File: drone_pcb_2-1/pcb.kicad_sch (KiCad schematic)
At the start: 3 parts, among them U1 MPU-6050, U3 ESP32-WROOM-32

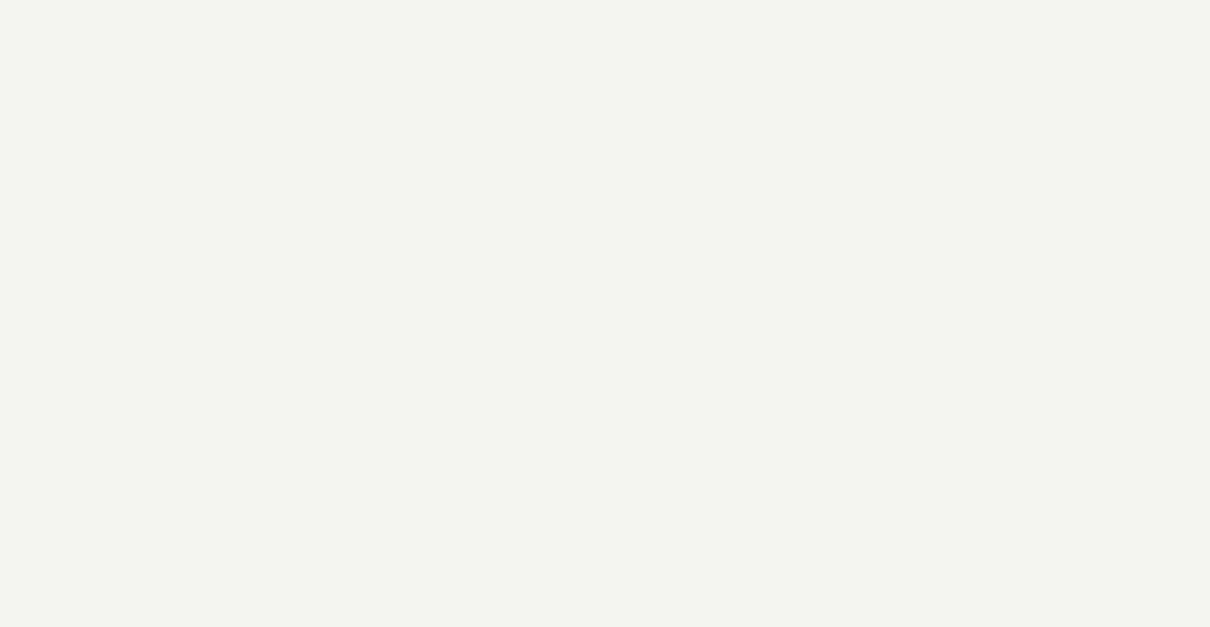
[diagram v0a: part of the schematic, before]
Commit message: add A5936 esc
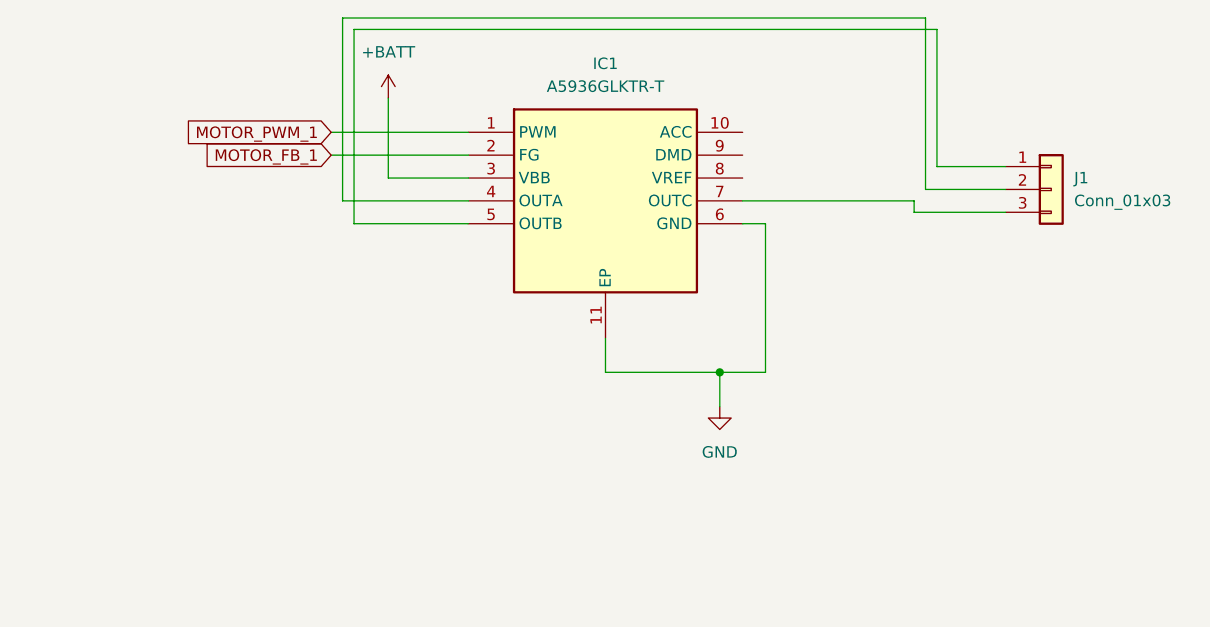
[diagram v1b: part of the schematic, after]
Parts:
- added IC1: A5936GLKTR-T, SOP100P600X165-11N, symbol A5936:A5936GLKTR-T
- added J1: Conn_01x03, symbol Connector_Generic:Conn_01x03
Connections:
- new net: IC1.5 (OUTB), J1.1 (Pin_1)
- new net: IC1.4 (OUTA), J1.2 (Pin_2)
- new net: IC1.7 (OUTC), J1.3 (Pin_3)
- new net +BATT: IC1.3 (VBB)
- new net GND: IC1.11 (EP), IC1.6 (GND)
- new net MOTOR_FB_1: IC1.2 (FG)
- new net MOTOR_PWM_1: IC1.1 (PWM)
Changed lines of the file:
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@@
 (kicad_sch (version 20230121) (generator eeschema)
   (paper "A3")
+  (junction (at 355.6 67.31) (diameter 0) (color 0 0 0 0)
+  )
+  (wire (pts (xy 313.69 27.94) (xy 378.46 27.94))
+    (stroke (width 0) (type default))
+  )
+  (wire (pts (xy 377.19 49.53) (xy 387.35 49.53))
+    (stroke (width 0) (type default))
+  )
+  (wire (pts (xy 378.46 27.94) (xy 378.46 46.99))
+    (stroke (width 0) (type default))
+  )
+  (wire (pts (xy 312.42 40.64) (xy 327.66 40.64))
+    (stroke (width 0) (type default))
+  )
+  (wire (pts (xy 379.73 29.21) (xy 379.73 44.45))
+    (stroke (width 0) (type default))
+  )
+  (wire (pts (xy 312.42 43.18) (xy 327.66 43.18))
+    (stroke (width 0) (type default))
+  )
+  (wire (pts (xy 314.96 50.8) (xy 314.96 29.21))
+    (stroke (width 0) (type default))
+  )
+  (wire (pts (xy 378.46 46.99) (xy 387.35 46.99))
+    (stroke (width 0) (type default))
+  )
+  (wire (pts (xy 327.66 50.8) (xy 314.96 50.8))
+    (stroke (width 0) (type default))
+  )
+  (wire (pts (xy 358.14 50.8) (xy 360.68 50.8))
+    (stroke (width 0) (type default))
+  )
+  (wire (pts (xy 327.66 48.26) (xy 313.69 48.26))
+    (stroke (width 0) (type default))
+  )
+  (wire (pts (xy 313.69 48.26) (xy 313.69 27.94))
+    (stroke (width 0) (type default))
+  )
+  (wire (pts (xy 327.66 45.72) (xy 318.77 45.72))
+    (stroke (width 0) (type default))
+  )
+  (wire (pts (xy 377.19 48.26) (xy 377.19 49.53))
+    (stroke (width 0) (type default))
+  )
+  (wire (pts (xy 342.9 63.5) (xy 342.9 67.31))
+    (stroke (width 0) (type default))
+  )
+  (wire (pts (xy 318.77 45.72) (xy 318.77 36.83))
+    (stroke (width 0) (type default))
+  )
+  (wire (pts (xy 379.73 44.45) (xy 387.35 44.45))
+    (stroke (width 0) (type default))
+  )
+  (wire (pts (xy 355.6 71.12) (xy 355.6 67.31))
+    (stroke (width 0) (type default))
+  )
+  (wire (pts (xy 358.14 48.26) (xy 377.19 48.26))
+    (stroke (width 0) (type default))
+  )
+  (wire (pts (xy 314.96 29.21) (xy 379.73 29.21))
+    (stroke (width 0) (type default))
+  )
+  (wire (pts (xy 342.9 67.31) (xy 355.6 67.31))
+    (stroke (width 0) (type default))
+  )
+  (wire (pts (xy 360.68 67.31) (xy 355.6 67.31))
+    (stroke (width 0) (type default))
+  )
+  (wire (pts (xy 360.68 50.8) (xy 360.68 67.31))
+    (stroke (width 0) (type default))
+  )
+  (global_label "MOTOR_PWM_1" (shape input) (at 312.42 40.64 180) (fields_autoplaced)
+    (effects (font (size 1.27 1.27)) (justify right))
+    (property "Intersheetrefs" "${INTERSHEET_REFS}" (at 295.8467 40.64 0)
+      (effects (font (size 1.27 1.27)) (justify right) hide)
+    )
+  )
+  (global_label "MOTOR_FB_1" (shape input) (at 312.42 43.18 180) (fields_autoplaced)
+    (effects (font (size 1.27 1.27)) (justify right))
+    (property "Intersheetrefs" "${INTERSHEET_REFS}" (at 297.6609 43.18 0)
+      (effects (font (size 1.27 1.27)) (justify right) hide)
+    )
+  )
+  (symbol (lib_id "Connector_Generic:Conn_01x03") (at 392.43 46.99 0) (unit 1)
+    (in_bom yes) (on_board yes) (dnp no) (fields_autoplaced)
+    (property "Reference" "J1" (at 394.97 45.72 0)
+      (effects (font (size 1.27 1.27)) (justify left))
+    )
+    (property "Value" "Conn_01x03" (at 394.97 48.26 0)
+      (effects (font (size 1.27 1.27)) (justify left))
+    )
+    (property "Footprint" "" (at 392.43 46.99 0)
+      (effects (font (size 1.27 1.27)) hide)
+    )
+    (property "Datasheet" "~" (at 392.43 46.99 0)
+      (effects (font (size 1.27 1.27)) hide)
+    )
+    (pin "1")
+    (pin "2")
+    (pin "3")
+    (instances
+      (project "pcb"
+        (path "/86dd2ef4-708d-4533-9384-626d9620d24d"
+          (reference "J1") (unit 1)
+        )
+      )
+    )
+  )
   (symbol (lib_id "RF_Module:DWM1000") (at 72.39 73.66 0) (unit 1)
     (in_bom yes) (on_board yes) (dnp no) (fields_autoplaced)
@@
         (path "/86dd2ef4-708d-4533-9384-626d9620d24d"
           (reference "DWM1") (unit 1)
+        )
+      )
+    )
+  )
+  (symbol (lib_id "power:+BATT") (at 318.77 36.83 0) (unit 1)
+    (in_bom yes) (on_board yes) (dnp no) (fields_autoplaced)
+    (property "Reference" "#PWR02" (at 318.77 40.64 0)
+      (effects (font (size 1.27 1.27)) hide)
+    )
+    (property "Value" "+BATT" (at 318.77 31.75 0)
+      (effects (font (size 1.27 1.27)))
+    )
+    (property "Footprint" "" (at 318.77 36.83 0)
+      (effects (font (size 1.27 1.27)) hide)
+    )
+    (property "Datasheet" "" (at 318.77 36.83 0)
+      (effects (font (size 1.27 1.27)) hide)
+    )
+    (pin "1")
+    (instances
+      (project "pcb"
+        (path "/86dd2ef4-708d-4533-9384-626d9620d24d"
+          (reference "#PWR02") (unit 1)
         )
       )
@@
         )
       )
+    )
+  )
+  (symbol (lib_id "A5936:A5936GLKTR-T") (at 327.66 40.64 0) (unit 1)
+    (in_bom yes) (on_board yes) (dnp no) (fields_autoplaced)
+    (property "Reference" "IC1" (at 342.9 33.02 0)
+      (effects (font (size 1.27 1.27)))
+    )
+    (property "Value" "A5936GLKTR-T" (at 342.9 35.56 0)
+      (effects (font (size 1.27 1.27)))
+    )
+    (property "Footprint" "SOP100P600X165-11N" (at 354.33 135.56 0)
+      (effects (font (size 1.27 1.27)) (justify left top) hide)
+    )
+    (property "Datasheet" "https://www.allegromicro.com/-/media/files/datasheets/a5936-datasheet.ashx" (at 354.33 235.56 0)
+      (effects (font (size 1.27 1.27)) (justify left top) hide)
+    )
+    (property "Height" "1.65" (at 354.33 435.56 0)
+      (effects (font (size 1.27 1.27)) (justify left top) hide)
+    )
+    (property "Manufacturer_Name" "Allegro Microsystems" (at 354.33 535.56 0)
+      (effects (font (size 1.27 1.27)) (justify left top) hide)
+    )
+    (property "Manufacturer_Part_Number" "A5936GLKTR-T" (at 354.33 635.56 0)
+      (effects (font (size 1.27 1.27)) (justify left top) hide)
+    )
+    (property "Mouser Part Number" "" (at 354.33 735.56 0)
+      (effects (font (size 1.27 1.27)) (justify left top) hide)
+    )
+    (property "Mouser Price/Stock" "" (at 354.33 835.56 0)
+      (effects (font (size 1.27 1.27)) (justify left top) hide)
+    )
+    (property "Arrow Part Number" "" (at 354.33 935.56 0)
+      (effects (font (size 1.27 1.27)) (justify left top) hide)
+    )
+    (property "Arrow Price/Stock" "" (at 354.33 1035.56 0)
+      (effects (font (size 1.27 1.27)) (justify left top) hide)
+    )
+    (pin "1")
+    (pin "10")
+    (pin "11")
+    (pin "2")
+    (pin "3")
+    (pin "4")
+    (pin "5")
+    (pin "6")
+    (pin "7")
+    (pin "8")
+    (pin "9")
+    (instances
+      (project "pcb"
+        (path "/86dd2ef4-708d-4533-9384-626d9620d24d"
+          (reference "IC1") (unit 1)
+        )
+      )
+    )
+  )
+  (symbol (lib_id "power:GND") (at 355.6 71.12 0) (unit 1)
+    (in_bom yes) (on_board yes) (dnp no) (fields_autoplaced)
+    (property "Reference" "#PWR01" (at 355.6 77.47 0)
+      (effects (font (size 1.27 1.27)) hide)
+    )
+    (property "Value" "GND" (at 355.6 76.2 0)
+      (effects (font (size 1.27 1.27)))
+    )
+    (property "Footprint" "" (at 355.6 71.12 0)
+      (effects (font (size 1.27 1.27)) hide)
+    )
+    (property "Datasheet" "" (at 355.6 71.12 0)
+      (effects (font (size 1.27 1.27)) hide)
+    )
+    (pin "1")
+    (instances
+      (project "pcb"
+        (path "/86dd2ef4-708d-4533-9384-626d9620d24d"
+          (reference "#PWR01") (unit 1)
+        )
+      )

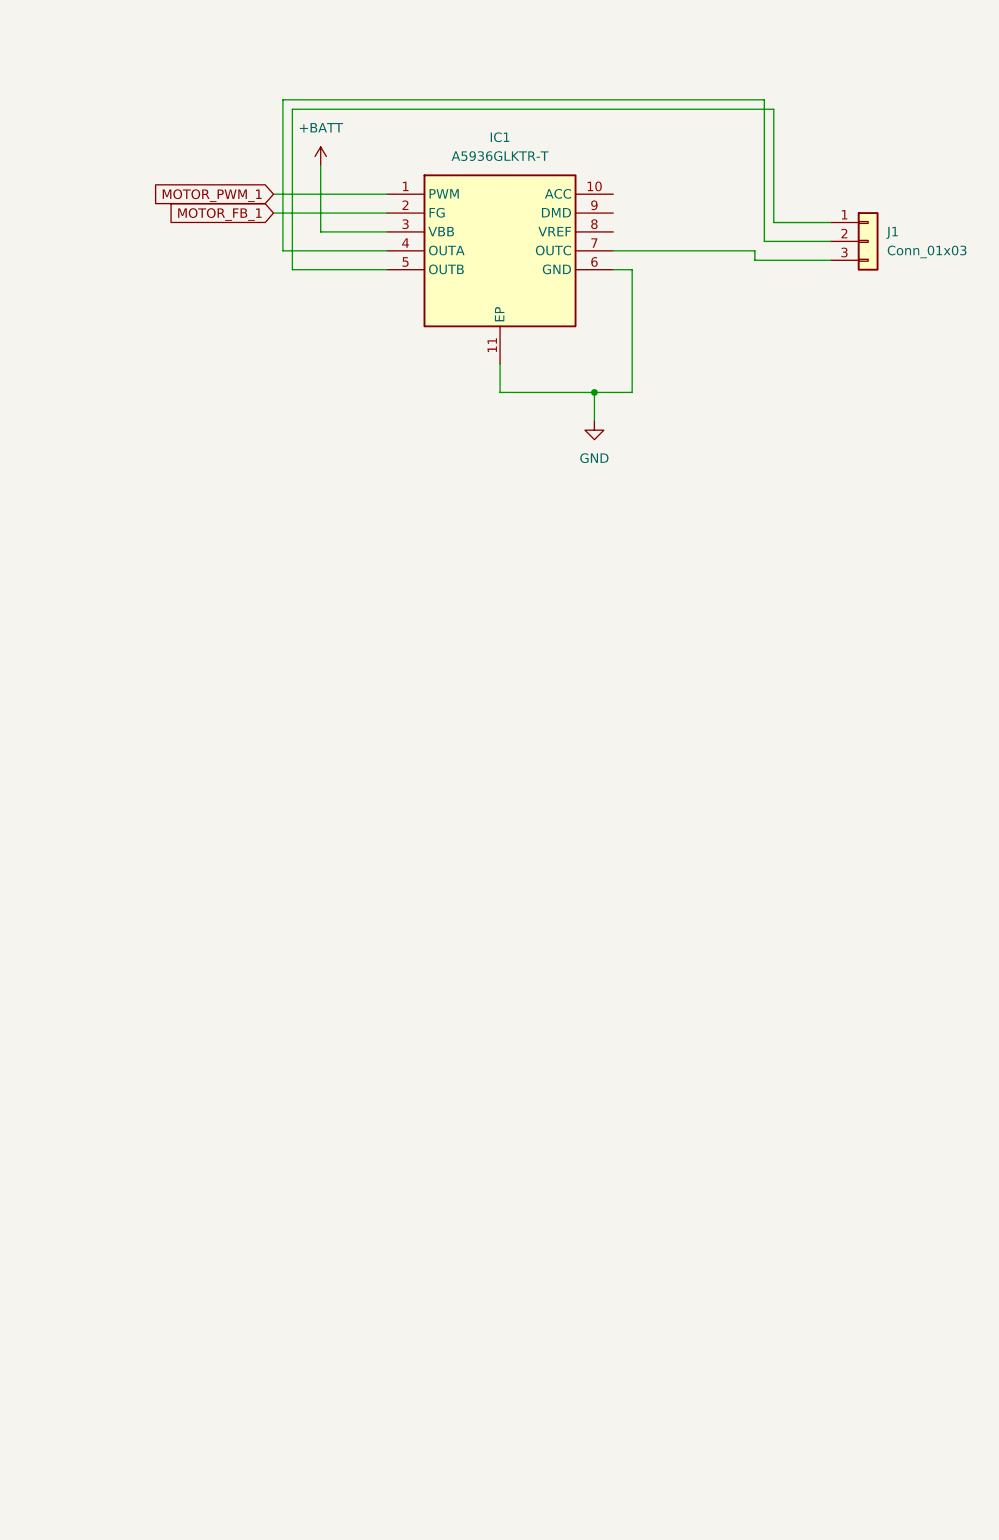
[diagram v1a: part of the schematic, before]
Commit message: add motor esc
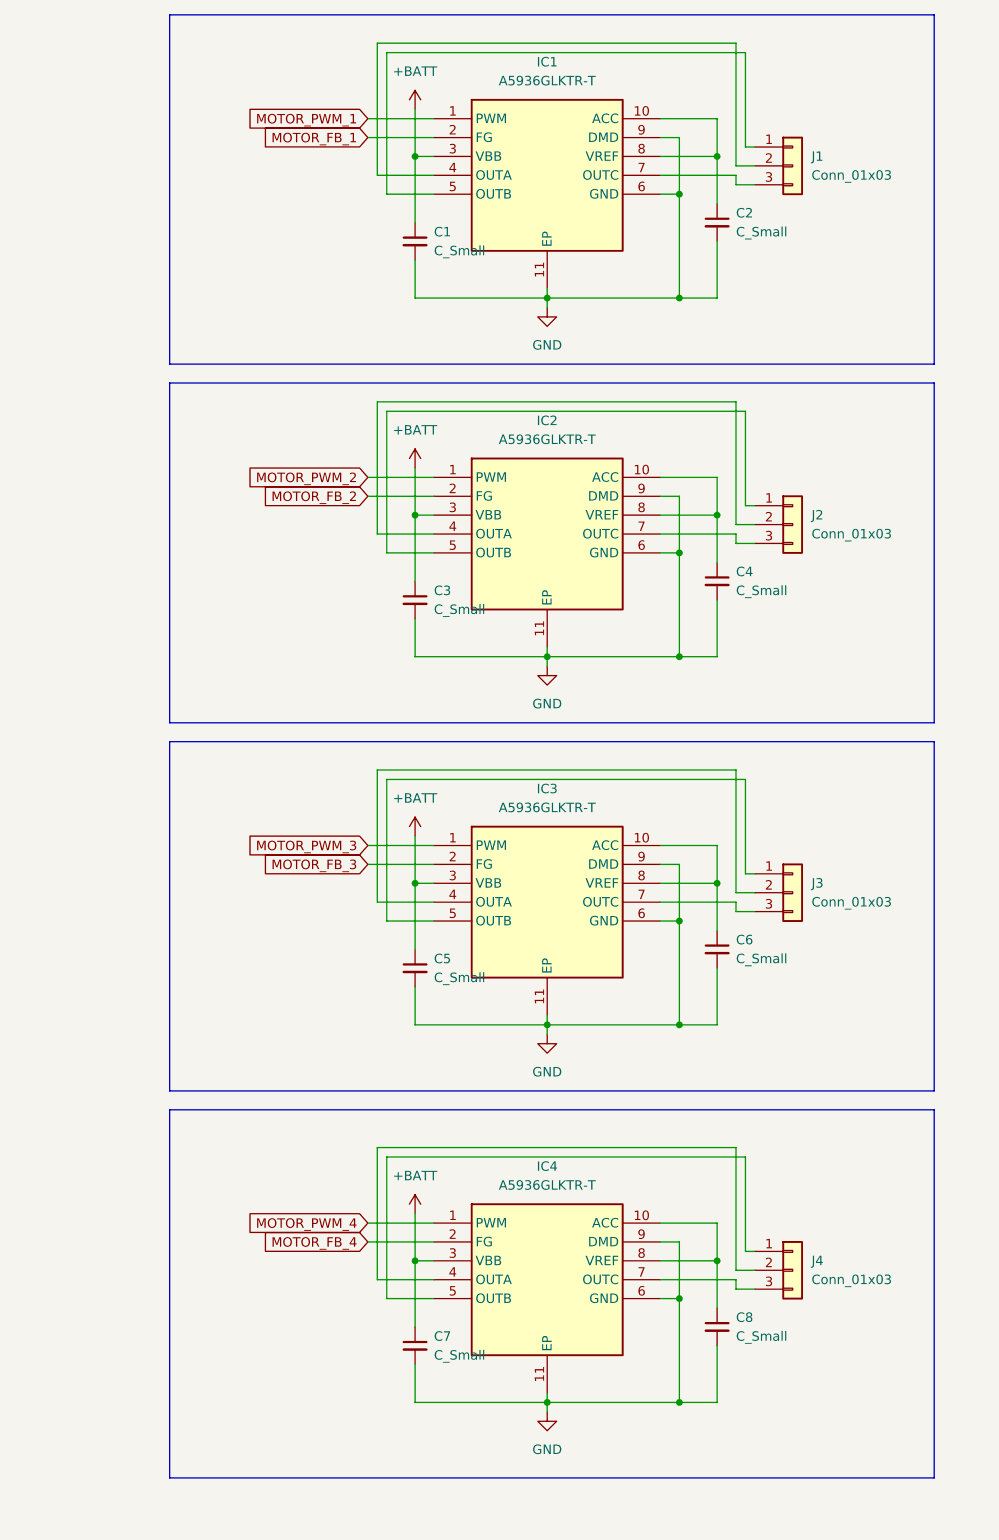
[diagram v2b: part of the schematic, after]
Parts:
- added C1, C2, C3, C4, C5, C6, C7, C8: C_Small, symbol Device:C_Small
- added IC2, IC3, IC4: A5936GLKTR-T, SOP100P600X165-11N, symbol A5936:A5936GLKTR-T
- added J2, J3, J4: Conn_01x03, symbol Connector_Generic:Conn_01x03
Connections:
- net +BATT: now also C1.1, C3.1, C5.1, C7.1, IC2.3 (VBB), IC3.3 (VBB), IC4.3 (VBB)
- net GND: now also IC1.9 (DMD), C1.2, C2.2, C3.2, C4.2, C5.2, C6.2, C7.2, C8.2, IC2.11 (EP), IC2.6 (GND), IC2.9 (DMD), IC3.11 (EP), IC3.6 (GND), IC3.9 (DMD), IC4.11 (EP), IC4.6 (GND), IC4.9 (DMD)
- net at IC1.10 (ACC): now also IC1.8 (VREF), C2.1
- new net: C4.1, IC2.10 (ACC), IC2.8 (VREF)
- new net: IC2.4 (OUTA), J2.2 (Pin_2)
- new net: IC2.5 (OUTB), J2.1 (Pin_1)
- new net: IC2.7 (OUTC), J2.3 (Pin_3)
- new net: C8.1, IC4.10 (ACC), IC4.8 (VREF)
- new net: IC4.4 (OUTA), J4.2 (Pin_2)
- new net: IC4.5 (OUTB), J4.1 (Pin_1)
- new net: IC4.7 (OUTC), J4.3 (Pin_3)
- new net: C6.1, IC3.10 (ACC), IC3.8 (VREF)
- new net: IC3.4 (OUTA), J3.2 (Pin_2)
- new net: IC3.5 (OUTB), J3.1 (Pin_1)
- new net: IC3.7 (OUTC), J3.3 (Pin_3)
- new net MOTOR_FB_2: IC2.2 (FG)
- new net MOTOR_FB_3: IC3.2 (FG)
- new net MOTOR_FB_4: IC4.2 (FG)
- new net MOTOR_PWM_2: IC2.1 (PWM)
- new net MOTOR_PWM_3: IC3.1 (PWM)
- new net MOTOR_PWM_4: IC4.1 (PWM)
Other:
- moved on the sheet: IC1, J1
